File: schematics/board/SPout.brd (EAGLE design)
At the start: 82 x 82 mm, 38 parts

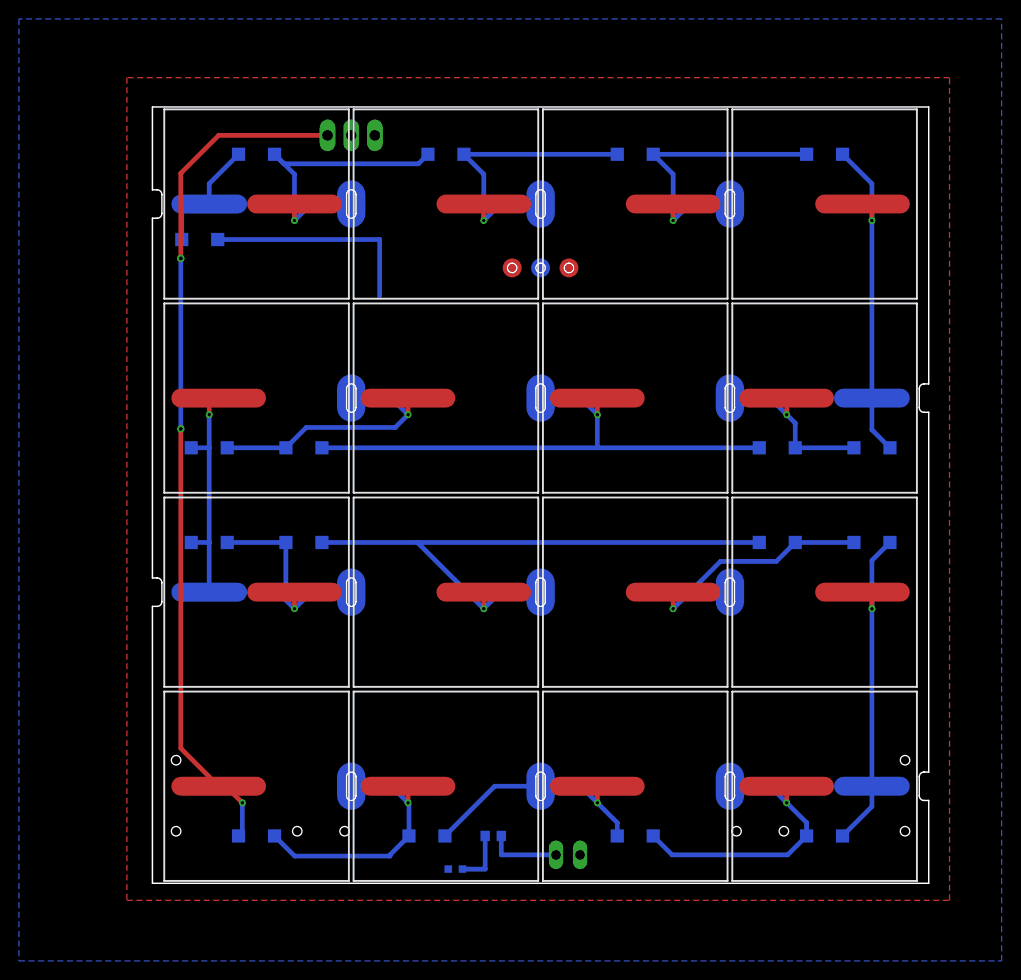
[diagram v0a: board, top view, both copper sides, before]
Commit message: Плата СП изменена для возможности подключения 2 вариантов ФЭПов
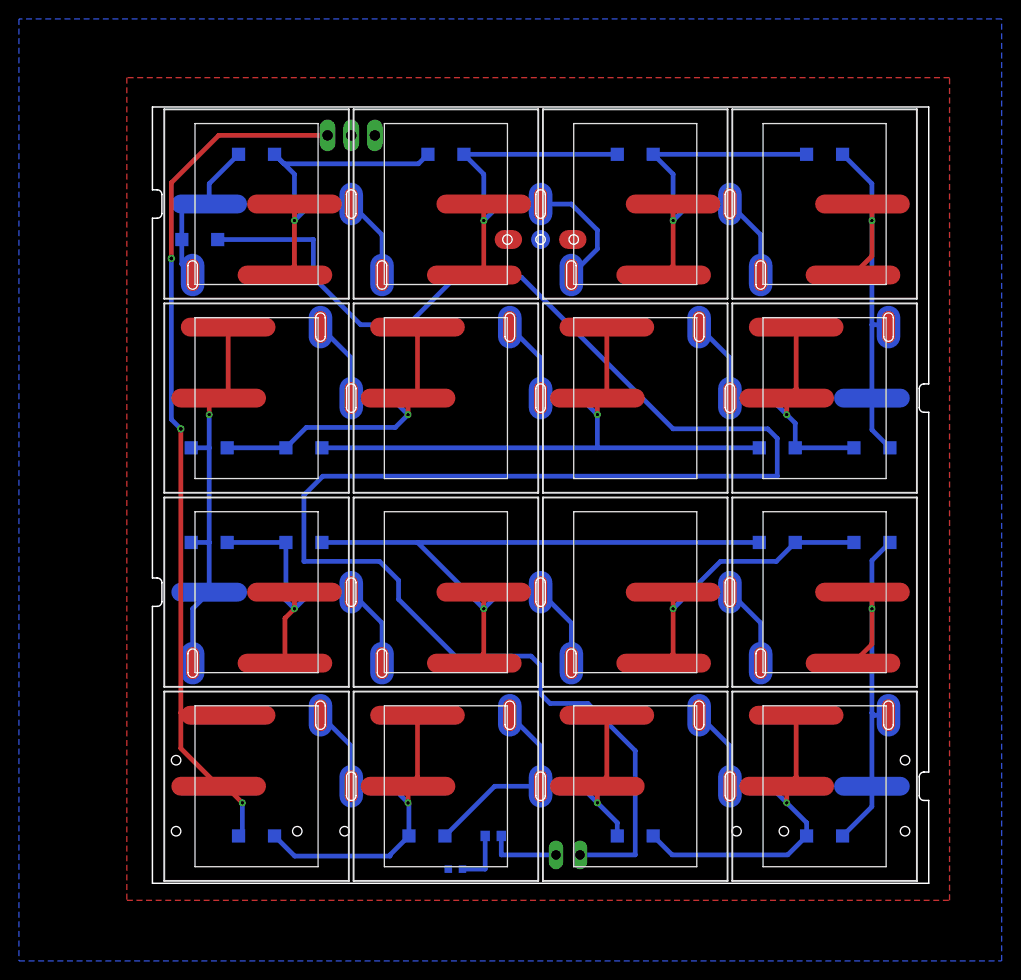
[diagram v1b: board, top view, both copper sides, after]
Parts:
- SOL1, SOL10, SOL11, SOL13, SOL14, SOL15, SOL2, SOL3, SOL5, SOL6, SOL7, SOL9: value SOLAR_0 -> SOLAR-2_0; device CanCubeSat:SOLAR_0 -> CanCubeSat:SOLAR_0-2
- SOL12, SOL16, SOL4, SOL8: value SOLAR_1 -> SOLAR-2_1; device CanCubeSat:SOLAR_1 -> CanCubeSat:SOLAR_1-2
- U$6: value GRAFITGRAFIT3_1 -> GRAFITGRAFIT4_2; device CanCubeSat:GRAFIT3_1 -> CanCubeSat:GRAFIT4_2
- moved U$6 3.00 mm to (41.0, 68.0)
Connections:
- net N$1: now also SOL1.OUT-2, SOL1.OUT-21, SOL1.OUT1, SOL2.IN-2
- net N$10: now also SOL7.OUT-2, SOL7.OUT-21, SOL7.OUT1, SOL8.IN-2
- net N$11: now also SOL8.OUT-2, SOL8.OUT-21, SOL9.IN-2
- net N$12: now also SOL10.IN-2, SOL9.OUT-2, SOL9.OUT-21, SOL9.OUT1
- net N$13: now also SOL10.OUT-2, SOL10.OUT-21, SOL10.OUT1, SOL11.IN-2
- net N$14: now also SOL11.OUT-2, SOL11.OUT-21, SOL11.OUT1, SOL12.IN-2
- net N$15: now also SOL12.OUT-2, SOL12.OUT-21, SOL13.IN-2
- net N$16: now also SOL13.OUT-2, SOL13.OUT-21, SOL13.OUT1, SOL14.IN-2
- net N$17: now also SOL14.OUT-2, SOL14.OUT-21, SOL14.OUT1, SOL15.IN-2
- net N$18: now also SOL15.OUT-2, SOL15.OUT-21, SOL15.OUT1, SOL16.IN-2
- net N$24: now also SOL4.OUT-2, SOL4.OUT-21, SOL5.IN-2
- net N$3: now also SOL2.OUT-2, SOL2.OUT-21, SOL2.OUT1, SOL3.IN-2
- net N$4: now also SOL16.OUT-2, SOL16.OUT-21
- net N$6: now also SOL3.OUT-2, SOL3.OUT-21, SOL3.OUT1, SOL4.IN-2
- net N$7: now also SOL1.IN-2
- net N$8: now also SOL5.OUT-2, SOL5.OUT-21, SOL5.OUT1, SOL6.IN-2
- net N$9: now also SOL6.OUT-2, SOL6.OUT-21, SOL6.OUT1, SOL7.IN-2
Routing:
- net BUS-: track 23.3 -> 199.3 mm
- net N$17: track 32.5 -> 54.1 mm
- net N$12: track 29.0 -> 46.0 mm
- net N$13: track 58.2 -> 75.2 mm
- net N$3: track 25.1 -> 41.9 mm
- net N$14: track 18.5 -> 35.3 mm
- net N$1: track 28.1 -> 44.8 mm
- net N$6: track 30.7 -> 47.5 mm
- net N$11: track 25.3 -> 41.7 mm
- net N$10: track 22.0 -> 37.1 mm
- net N$8: track 28.0 -> 43.0 mm
- net N$18: track 33.4 -> 48.4 mm
- net N$16: track 32.5 -> 47.6 mm
- net N$9: track 64.6 -> 79.6 mm
- net N$24: track 35.8 -> 44.3 mm
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
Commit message: Добавлены подписи Концерна к платам
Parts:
- added U$26: PCB "Solar Panel", CanCubeSat:ITS-LOGO
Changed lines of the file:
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@@
 <drawing>
 <settings>
-<setting alwaysvectorfont="no"/>
+<setting alwaysvectorfont="yes"/>
 <setting verticaltext="up"/>
 </settings>
 <grid distance="1" unitdist="mm" unit="mm" style="lines" multiple="1" display="yes" altdistance="0.25" altunitdist="mm" altunit="mm"/>
 <layers>
-<layer number="1" name="Top" color="4" fill="1" visible="yes" active="yes"/>
+<layer number="1" name="Top" color="4" fill="1" visible="no" active="yes"/>
 <layer number="2" name="Route2" color="16" fill="1" visible="no" active="yes"/>
 <layer number="3" name="Route3" color="17" fill="1" visible="no" active="yes"/>
@@
 <layer number="13" name="Route13" color="21" fill="1" visible="no" active="yes"/>
 <layer number="14" name="Route14" color="22" fill="1" visible="no" active="yes"/>
-<layer number="15" name="Route15" color="23" fill="1" visible="yes" active="yes"/>
+<layer number="15" name="Route15" color="23" fill="1" visible="no" active="yes"/>
 <layer number="16" name="Bottom" color="1" fill="1" visible="yes" active="yes"/>
 <layer number="17" name="Pads" color="2" fill="1" visible="yes" active="yes"/>
@@
 <layer number="19" name="Unrouted" color="6" fill="1" visible="yes" active="yes"/>
 <layer number="20" name="Dimension" color="24" fill="1" visible="yes" active="yes"/>
-<layer number="21" name="tPlace" color="7" fill="1" visible="yes" active="yes"/>
+<layer number="21" name="tPlace" color="7" fill="1" visible="no" active="yes"/>
 <layer number="22" name="bPlace" color="7" fill="1" visible="yes" active="yes"/>
-<layer number="23" name="tOrigins" color="15" fill="1" visible="yes" active="yes"/>
+<layer number="23" name="tOrigins" color="15" fill="1" visible="no" active="yes"/>
 <layer number="24" name="bOrigins" color="15" fill="1" visible="yes" active="yes"/>
-<layer number="25" name="tNames" color="7" fill="1" visible="yes" active="yes"/>
+<layer number="25" name="tNames" color="7" fill="1" visible="no" active="yes"/>
 <layer number="26" name="bNames" color="7" fill="1" visible="yes" active="yes"/>
 <layer number="27" name="tValues" color="7" fill="1" visible="no" active="yes"/>
@@
 <layer number="37" name="tTest" color="7" fill="1" visible="no" active="yes"/>
 <layer number="38" name="bTest" color="7" fill="1" visible="no" active="yes"/>
-<layer number="39" name="tKeepout" color="4" fill="11" visible="yes" active="yes"/>
+<layer number="39" name="tKeepout" color="4" fill="11" visible="no" active="yes"/>
 <layer number="40" name="bKeepout" color="1" fill="11" visible="yes" active="yes"/>
-<layer number="41" name="tRestrict" color="4" fill="10" visible="yes" active="yes"/>
+<layer number="41" name="tRestrict" color="4" fill="10" visible="no" active="yes"/>
 <layer number="42" name="bRestrict" color="1" fill="10" visible="yes" active="yes"/>
 <layer number="43" name="vRestrict" color="2" fill="10" visible="no" active="yes"/>
 <layer number="44" name="Drills" color="7" fill="1" visible="no" active="yes"/>
-<layer number="45" name="Holes" color="7" fill="1" visible="yes" active="yes"/>
+<layer number="45" name="Holes" color="7" fill="1" visible="no" active="yes"/>
 <layer number="46" name="Milling" color="3" fill="1" visible="no" active="yes"/>
 <layer number="47" name="Measures" color="7" fill="1" visible="no" active="yes"/>
@@
 <layer number="49" name="Reference" color="7" fill="1" visible="no" active="yes"/>
 <layer number="50" name="dxf" color="7" fill="1" visible="no" active="yes"/>
-<layer number="51" name="tDocu" color="7" fill="1" visible="yes" active="yes"/>
+<layer number="51" name="tDocu" color="7" fill="1" visible="no" active="yes"/>
 <layer number="52" name="bDocu" color="7" fill="1" visible="yes" active="yes"/>
 <layer number="53" name="tGND_GNDA" color="7" fill="9" visible="no" active="no"/>
@@
 </element>
 <element name="U$6" library="CanCubeSat" package="GRAFIT4_2" value="GRAFITGRAFIT4_2" x="41" y="68" smashed="yes" rot="R90"/>
+<element name="U$26" library="CanCubeSat" package="ITS-LOGO" value="PCB &quot;Solar Panel&quot;" x="10" y="50" smashed="yes" rot="MR90">
+<attribute name="VALUE" x="8.5" y="50" size="1" layer="22" font="vector" ratio="15" rot="MR90"/>
+</element>
 </elements>
 <signals>

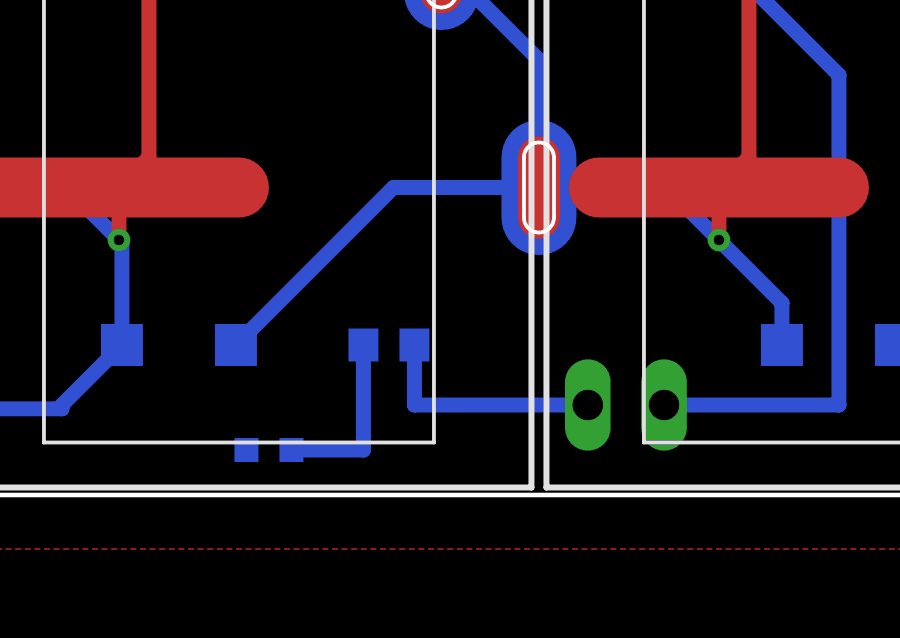
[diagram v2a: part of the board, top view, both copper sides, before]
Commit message: Добавлен конденсатор на питание СБ
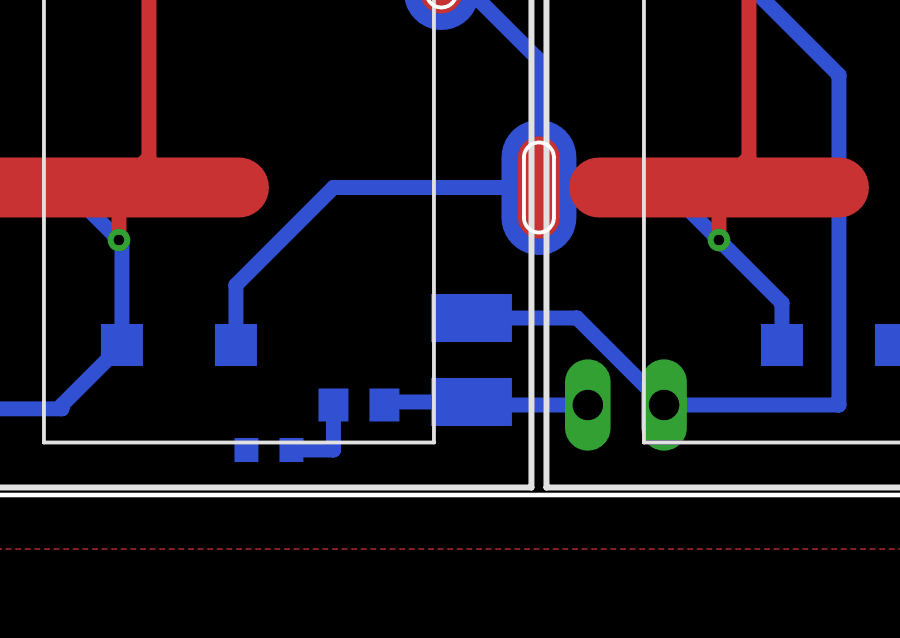
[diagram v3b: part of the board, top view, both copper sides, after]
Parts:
- added C1: 47µ, rcl:C1210
- moved R1_2K7 2.24 mm to (35.0, 3.00)
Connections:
- net BUS+: now also C1.2
- net BUS-: now also C1.1
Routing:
- net BUS-: track 199.3 -> 206.9 mm
- net N$5: track 5.90 -> 2.90 mm
- net N$3: track 41.9 -> 43.1 mm
- net BUS+: track 7.78 -> 6.86 mm
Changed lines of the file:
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@@
 <grid distance="1" unitdist="mm" unit="mm" style="lines" multiple="1" display="yes" altdistance="0.25" altunitdist="mm" altunit="mm"/>
 <layers>
-<layer number="1" name="Top" color="4" fill="1" visible="no" active="yes"/>
-<layer number="2" name="Route2" color="16" fill="1" visible="no" active="yes"/>
-<layer number="3" name="Route3" color="17" fill="1" visible="no" active="yes"/>
-<layer number="4" name="Route4" color="18" fill="1" visible="no" active="yes"/>
-<layer number="5" name="Route5" color="19" fill="1" visible="no" active="yes"/>
-<layer number="6" name="Route6" color="25" fill="1" visible="no" active="yes"/>
-<layer number="7" name="Route7" color="26" fill="1" visible="no" active="yes"/>
-<layer number="8" name="Route8" color="27" fill="1" visible="no" active="yes"/>
-<layer number="9" name="Route9" color="28" fill="1" visible="no" active="yes"/>
-<layer number="10" name="Route10" color="29" fill="1" visible="no" active="yes"/>
-<layer number="11" name="Route11" color="30" fill="1" visible="no" active="yes"/>
-<layer number="12" name="Route12" color="20" fill="1" visible="no" active="yes"/>
-<layer number="13" name="Route13" color="21" fill="1" visible="no" active="yes"/>
-<layer number="14" name="Route14" color="22" fill="1" visible="no" active="yes"/>
-<layer number="15" name="Route15" color="23" fill="1" visible="no" active="yes"/>
+<layer number="1" name="Top" color="4" fill="1" visible="yes" active="yes"/>
+<layer number="2" name="Route2" color="16" fill="1" visible="yes" active="yes"/>
+<layer number="3" name="Route3" color="17" fill="1" visible="yes" active="yes"/>
+<layer number="4" name="Route4" color="18" fill="1" visible="yes" active="yes"/>
+<layer number="5" name="Route5" color="19" fill="1" visible="yes" active="yes"/>
+<layer number="6" name="Route6" color="25" fill="1" visible="yes" active="yes"/>
+<layer number="7" name="Route7" color="26" fill="1" visible="yes" active="yes"/>
+<layer number="8" name="Route8" color="27" fill="1" visible="yes" active="yes"/>
+<layer number="9" name="Route9" color="28" fill="1" visible="yes" active="yes"/>
+<layer number="10" name="Route10" color="29" fill="1" visible="yes" active="yes"/>
+<layer number="11" name="Route11" color="30" fill="1" visible="yes" active="yes"/>
+<layer number="12" name="Route12" color="20" fill="1" visible="yes" active="yes"/>
+<layer number="13" name="Route13" color="21" fill="1" visible="yes" active="yes"/>
+<layer number="14" name="Route14" color="22" fill="1" visible="yes" active="yes"/>
+<layer number="15" name="Route15" color="23" fill="1" visible="yes" active="yes"/>
 <layer number="16" name="Bottom" color="1" fill="1" visible="yes" active="yes"/>
 <layer number="17" name="Pads" color="2" fill="1" visible="yes" active="yes"/>
@@
 <layer number="19" name="Unrouted" color="6" fill="1" visible="yes" active="yes"/>
 <layer number="20" name="Dimension" color="24" fill="1" visible="yes" active="yes"/>
-<layer number="21" name="tPlace" color="7" fill="1" visible="no" active="yes"/>
+<layer number="21" name="tPlace" color="7" fill="1" visible="yes" active="yes"/>
 <layer number="22" name="bPlace" color="7" fill="1" visible="yes" active="yes"/>
-<layer number="23" name="tOrigins" color="15" fill="1" visible="no" active="yes"/>
+<layer number="23" name="tOrigins" color="15" fill="1" visible="yes" active="yes"/>
 <layer number="24" name="bOrigins" color="15" fill="1" visible="yes" active="yes"/>
-<layer number="25" name="tNames" color="7" fill="1" visible="no" active="yes"/>
+<layer number="25" name="tNames" color="7" fill="1" visible="yes" active="yes"/>
 <layer number="26" name="bNames" color="7" fill="1" visible="yes" active="yes"/>
 <layer number="27" name="tValues" color="7" fill="1" visible="no" active="yes"/>
@@
 <layer number="37" name="tTest" color="7" fill="1" visible="no" active="yes"/>
 <layer number="38" name="bTest" color="7" fill="1" visible="no" active="yes"/>
-<layer number="39" name="tKeepout" color="4" fill="11" visible="no" active="yes"/>
+<layer number="39" name="tKeepout" color="4" fill="11" visible="yes" active="yes"/>
 <layer number="40" name="bKeepout" color="1" fill="11" visible="yes" active="yes"/>
-<layer number="41" name="tRestrict" color="4" fill="10" visible="no" active="yes"/>
+<layer number="41" name="tRestrict" color="4" fill="10" visible="yes" active="yes"/>
 <layer number="42" name="bRestrict" color="1" fill="10" visible="yes" active="yes"/>
 <layer number="43" name="vRestrict" color="2" fill="10" visible="no" active="yes"/>
@@
 <layer number="49" name="Reference" color="7" fill="1" visible="no" active="yes"/>
 <layer number="50" name="dxf" color="7" fill="1" visible="no" active="yes"/>
-<layer number="51" name="tDocu" color="7" fill="1" visible="no" active="yes"/>
+<layer number="51" name="tDocu" color="7" fill="1" visible="yes" active="yes"/>
 <layer number="52" name="bDocu" color="7" fill="1" visible="yes" active="yes"/>
 <layer number="53" name="tGND_GNDA" color="7" fill="9" visible="no" active="no"/>
@@
 <attribute name="VALUE" x="21" y="82.556" size="1.27" layer="28" ratio="10" rot="MR0"/>
 </element>
-<element name="R1_2K7" library="rcl" library_urn="urn:adsk.eagle:library:334" package="R0603" package3d_urn="urn:adsk.eagle:package:23555/3" value="2k7" x="36" y="5" smashed="yes" rot="MR0">
-<attribute name="NAME" x="38.139" y="6.206" size="1.27" layer="26" rot="MR0"/>
-<attribute name="POPULARITY" value="77" x="36" y="5" size="1.778" layer="28" rot="MR0" display="off"/>
-<attribute name="SPICEPREFIX" value="R" x="36" y="5" size="1.778" layer="28" rot="MR0" display="off"/>
-<attribute name="VALUE" x="36.635" y="3.095" size="1.27" layer="28" rot="MR0"/>
+<element name="R1_2K7" library="rcl" library_urn="urn:adsk.eagle:library:334" package="R0603" package3d_urn="urn:adsk.eagle:package:23555/3" value="2k7" x="35" y="3" smashed="yes" rot="MR0">
+<attribute name="NAME" x="37.139" y="4.206" size="1.27" layer="26" rot="MR0"/>
+<attribute name="POPULARITY" value="77" x="35" y="3" size="1.778" layer="28" rot="MR0" display="off"/>
+<attribute name="SPICEPREFIX" value="R" x="35" y="3" size="1.778" layer="28" rot="MR0" display="off"/>
+<attribute name="VALUE" x="35.635" y="1.095" size="1.27" layer="28" rot="MR0"/>
 </element>
 <element name="PWR" library="led" library_urn="urn:adsk.eagle:library:259" package="CHIPLED_0603" package3d_urn="urn:adsk.eagle:package:15822/2" value="" x="32" y="1.5" smashed="yes" rot="MR270">
@@
 <element name="U$26" library="CanCubeSat" package="ITS-LOGO" value="PCB &quot;Solar Panel&quot;" x="10" y="50" smashed="yes" rot="MR90">
 <attribute name="VALUE" x="8.5" y="50" size="1" layer="22" font="vector" ratio="15" rot="MR90"/>
+</element>
+<element name="C1" library="rcl" library_urn="urn:adsk.eagle:library:334" package="C1210" package3d_urn="urn:adsk.eagle:package:23619/2" value="47µ" x="38.75" y="4.5" smashed="yes" rot="MR270">
+<attribute name="NAME" x="36.845" y="6.405" size="1.27" layer="26" rot="MR270"/>
+<attribute name="POPULARITY" value="0" x="38.75" y="4.5" size="1.778" layer="28" rot="MR270" display="off"/>
+<attribute name="SPICEPREFIX" value="C" x="38.75" y="4.5" size="1.778" layer="28" rot="MR270" display="off"/>
+<attribute name="VALUE" x="41.925" y="6.405" size="1.27" layer="28" rot="MR270"/>
 </element>
 </elements>
@@
 <contactref element="JP1" pad="2"/>
 <contactref element="R1_2K7" pad="1"/>
-<wire x1="42.63" y1="3" x2="36.85" y2="3" width="0.5" layer="16"/>
-<wire x1="36.85" y1="3" x2="36.85" y2="5" width="0.5" layer="16"/>
+<contactref element="C1" pad="2"/>
+<wire x1="42.63" y1="3" x2="38.85" y2="3" width="0.5" layer="16"/>
+<wire x1="38.85" y1="3" x2="38.75" y2="3.1" width="0.5" layer="16"/>
+<wire x1="38.75" y1="3.1" x2="35.95" y2="3.1" width="0.5" layer="16"/>
+<wire x1="35.95" y1="3.1" x2="35.85" y2="3" width="0.5" layer="16"/>
 </signal>
 <signal name="N$7">
@@
 <wire x1="49.1" y1="5" x2="49.1" y2="6.4" width="0.5" layer="16"/>
 <wire x1="49.1" y1="6.4" x2="47" y2="8.5" width="0.5" layer="16"/>
-<wire x1="36.15" y1="10.25" x2="30.9" y2="5" width="0.5" layer="16"/>
+<wire x1="34.15" y1="10.25" x2="30.9" y2="7" width="0.5" layer="16"/>
+<wire x1="30.9" y1="7" x2="30.9" y2="5" width="0.5" layer="16"/>
 <contactref element="SOL3" pad="IN-2"/>
 <contactref element="SOL2" pad="OUT-2"/>
@@
 <wire x1="48" y1="11.25" x2="47" y2="10.25" width="0.5" layer="1"/>
 <wire x1="41" y1="10.25" x2="45.25" y2="10.25" width="0.5" layer="16"/>
-<wire x1="41" y1="10.25" x2="36.15" y2="10.25" width="0.5" layer="16"/>
+<wire x1="41" y1="10.25" x2="34.15" y2="10.25" width="0.5" layer="16"/>
 <wire x1="41" y1="14.5" x2="41" y2="10.25" width="0.5" layer="16"/>
 <wire x1="37.75" y1="17.75" x2="41" y2="14.5" width="0.5" layer="16"/>
@@
 <wire x1="39" y1="64" x2="32" y2="64" width="0.5" layer="16"/>
 <wire x1="22" y1="59" x2="17" y2="64" width="0.5" layer="16"/>
+<contactref element="C1" pad="1"/>
+<wire x1="45.17" y1="3" x2="42.27" y2="5.9" width="0.5" layer="16"/>
+<wire x1="42.27" y1="5.9" x2="38.75" y2="5.9" width="0.5" layer="16"/>
 </signal>
 <signal name="N$4">
@@
 <contactref element="PWR" pad="A"/>
 <contactref element="R1_2K7" pad="2"/>
-<wire x1="32.75" y1="1.5" x2="35.15" y2="1.5" width="0.5" layer="16"/>
-<wire x1="35.15" y1="1.5" x2="35.15" y2="5" width="0.5" layer="16"/>
+<wire x1="32.75" y1="1.5" x2="34.15" y2="1.5" width="0.5" layer="16"/>
+<wire x1="34.15" y1="1.5" x2="34.15" y2="3" width="0.5" layer="16"/>
 </signal>
 </signals>

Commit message: Добавлена шелкография на платах БСК и СП
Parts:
- renumbered R1_2K7 to 2K7
